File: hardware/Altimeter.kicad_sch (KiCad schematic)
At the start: 6 parts, among them U13 SCH1633-D01

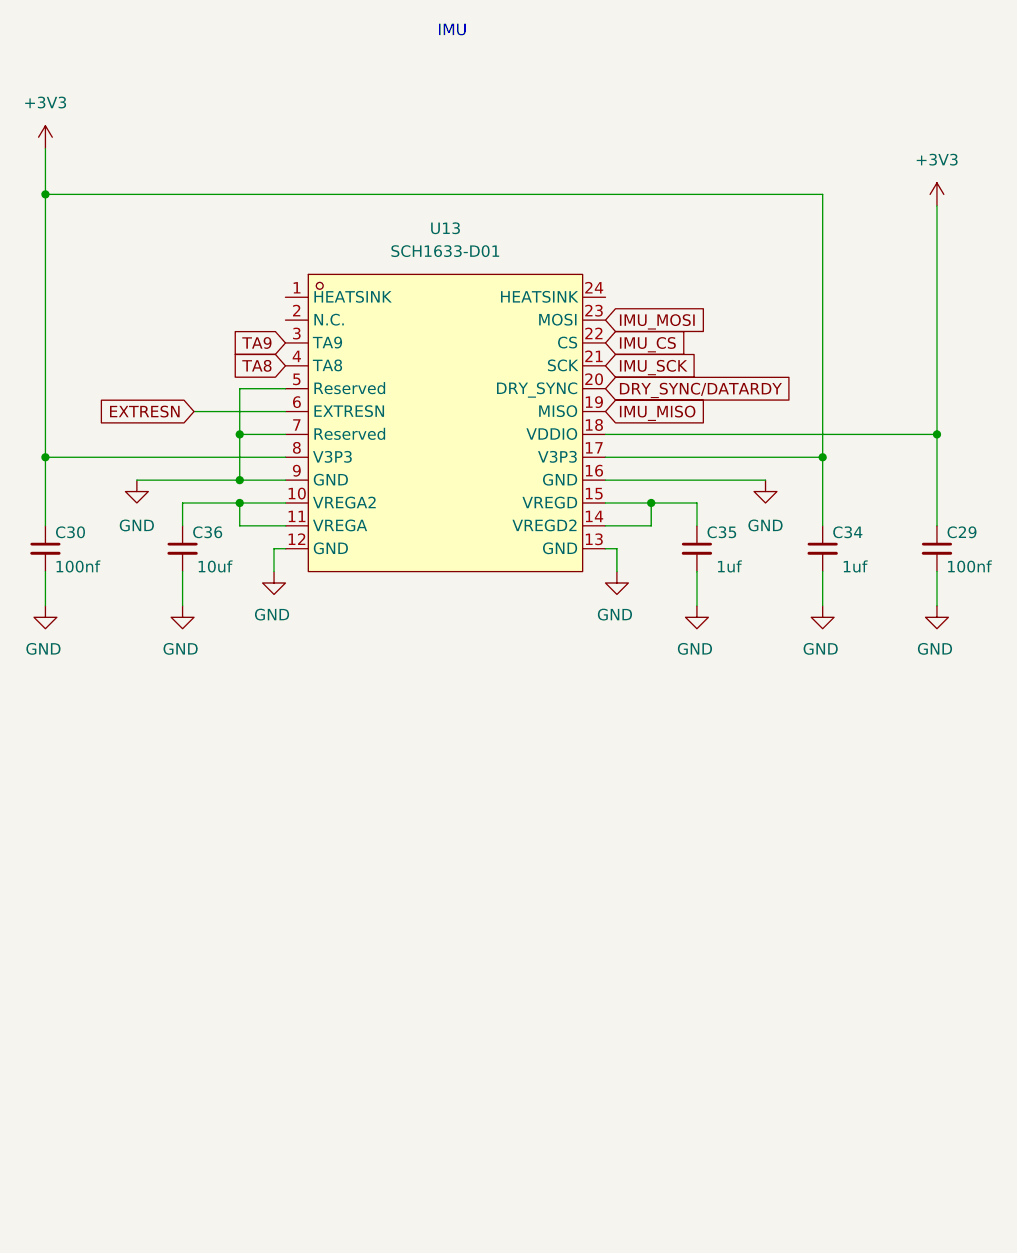
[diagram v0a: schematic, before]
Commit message: wire up altimeter, temp, barometer, imu, gps to MCU
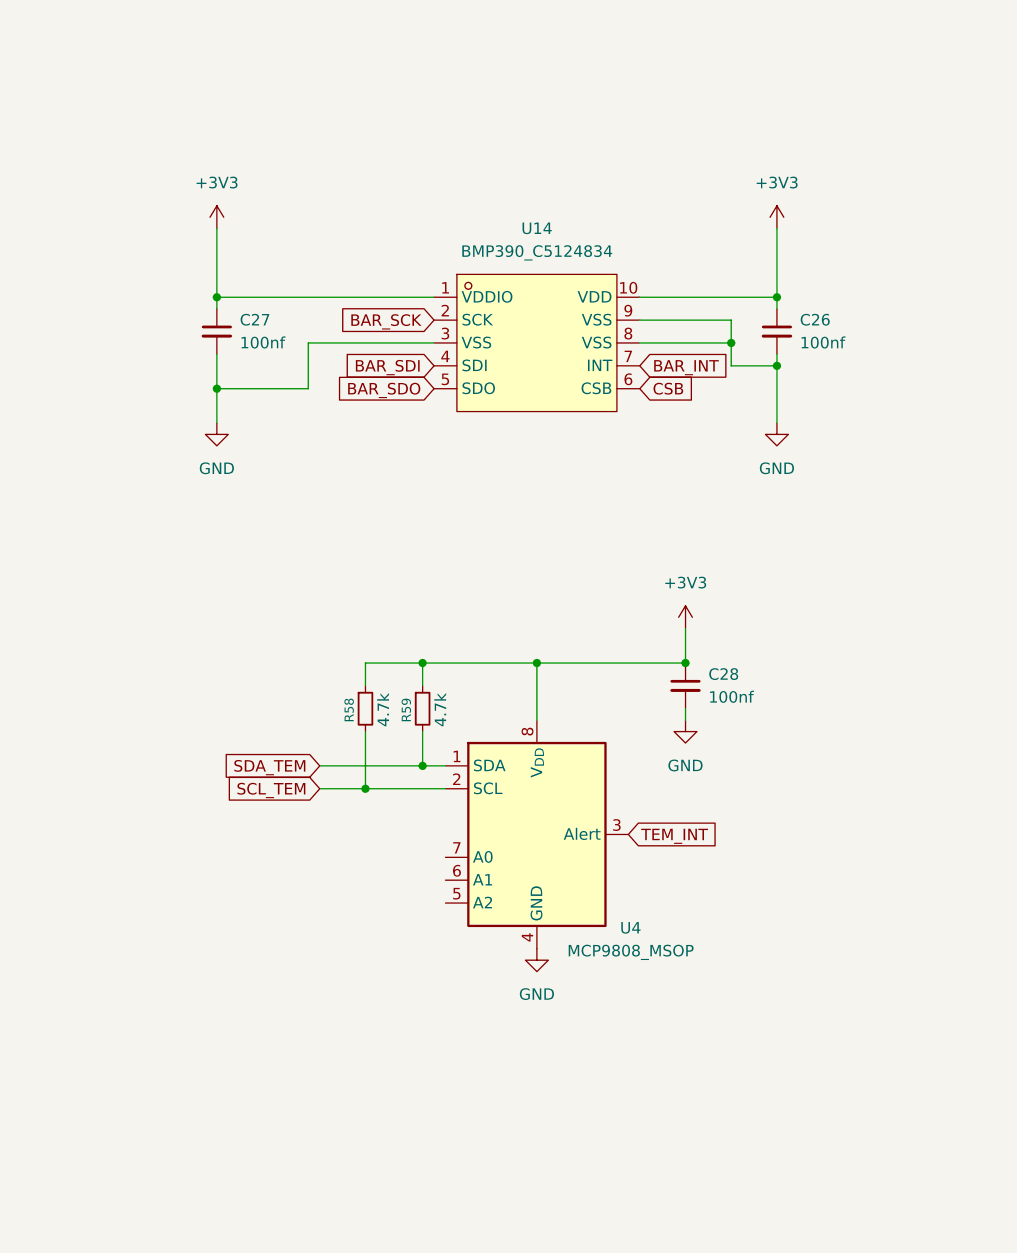
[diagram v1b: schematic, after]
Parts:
- removed C29, C30: 100nf, symbol Device:C_Small
- removed C34, C35: 1uf, symbol Device:C_Small
- removed C36: 10uf, symbol Device:C_Small
- removed U13: SCH1633-D01, EasyEDA:SOIC-24_L11.8-W9.8-P0.80-LS13.4-BL_SCH16T-K01, symbol Lib_Loader:SCH1633-D01
- added C26, C27, C28: 100nf, symbol Device:C_Small
- added R58, R59: 4.7k, symbol Device:R_Small
- added U14: BMP390_C5124834, ImpartGUI:LGA-10_L2.0-W2.0-P0.50-BL, symbol ImpartGUI:BMP390_C5124834
- added U4: MCP9808_MSOP, Package_SO:MSOP-8_3x3mm_P0.65mm, symbol Sensor_Temperature:MCP9808_MSOP
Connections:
- net +3V3: now also C26.1, C27.1, C28.1, R58.1, R59.1, U14.1 (VDDIO), U14.10 (VDD), U4.8 (V_{DD})
- net GND: now also C26.2, C27.2, C28.2, U14.3 (VSS), U14.8 (VSS), U14.9 (VSS), U4.4 (GND)
- new net BAR_INT: U14.7 (INT)
- new net BAR_SCK: U14.2 (SCK)
- new net BAR_SDI: U14.4 (SDI)
- new net BAR_SDO: U14.5 (SDO)
- new net CSB: U14.6 (CSB)
- new net SCL_TEM: R58.2, U4.2 (SCL)
- new net SDA_TEM: R59.2, U4.1 (SDA)
- new net TEM_INT: U4.3 (Alert)
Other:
- note removed: "IMU"

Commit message: fixed electrical rules
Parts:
- C26, C27, C28: footprint (none) -> Capacitor_SMD:C_0402_1005Metric
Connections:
- no-connect marks 0 -> 3
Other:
- note added: "BAROMETER"
- note added: "TEMPERATURE"
- moved on the sheet: C28, R58, R59, U4
